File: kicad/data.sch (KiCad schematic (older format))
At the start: 58 parts, among them J2 USB_B, J3 FTDI header, J4 PTT choice, J5 XCVR_CAT_TTL, J6 XCVR_PTT, U3 SN65220, U4 Si8663AB-B-IS1, U5 FT232RL, U6 SN74HCT32D, U7 VOR1121B6T

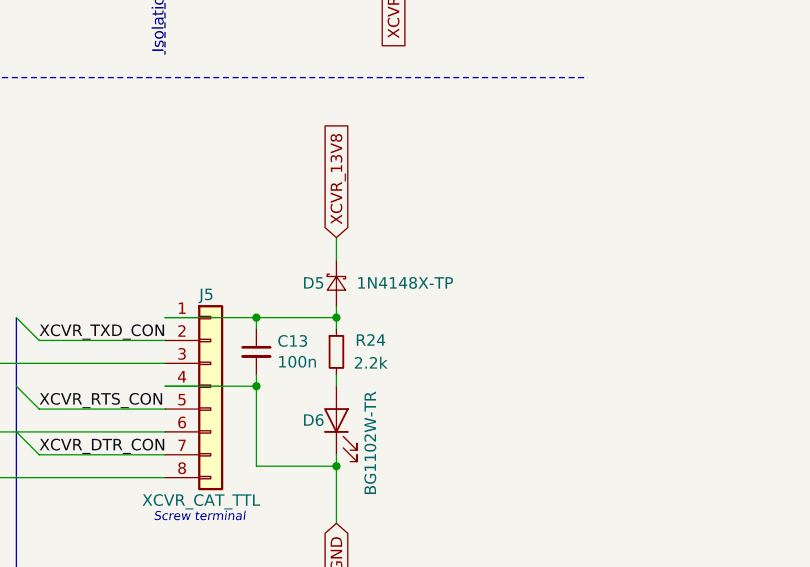
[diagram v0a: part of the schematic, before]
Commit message: Small fixes
* Moved via that was unreasonably close to another one
* Changed 13V8 diodes to SM5819PL-TP
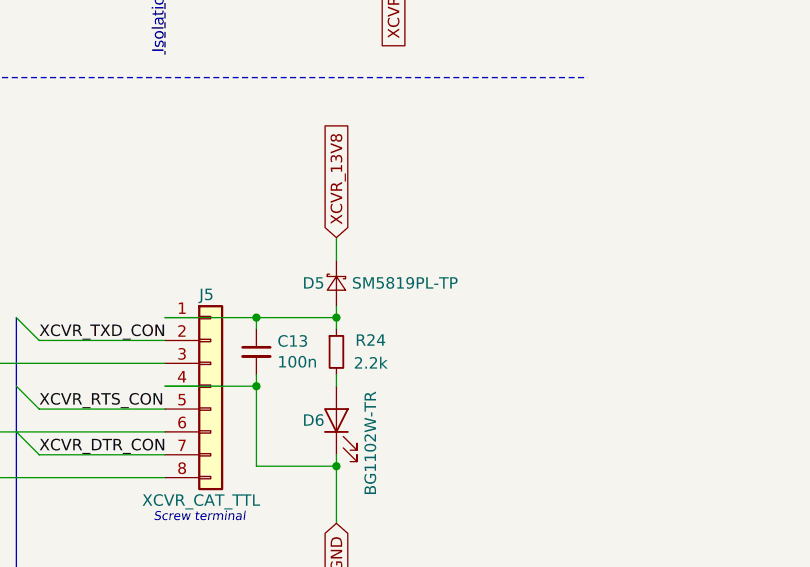
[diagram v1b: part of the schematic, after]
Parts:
- D5: value 1N4148X-TP -> SM5819PL-TP; footprint Diode_SMD:D_SOD-523 -> Diode_SMD:D_SOD-123F
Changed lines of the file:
@@
 P 10100 2900
 F 0 "D5" V 10100 3000 50  0000 C CNN
-F 1 "1N4148X-TP" V 10100 2600 50  0000 C CNN
-F 2 "Diode_SMD:D_SOD-523" V 10100 2900 50  0001 C CNN
+F 1 "SM5819PL-TP" V 10100 2600 50  0000 C CNN
+F 2 "Diode_SMD:D_SOD-123F" V 10100 2900 50  0001 C CNN
 F 3 "~" V 10100 2900 50  0001 C CNN
 	1    10100 2900

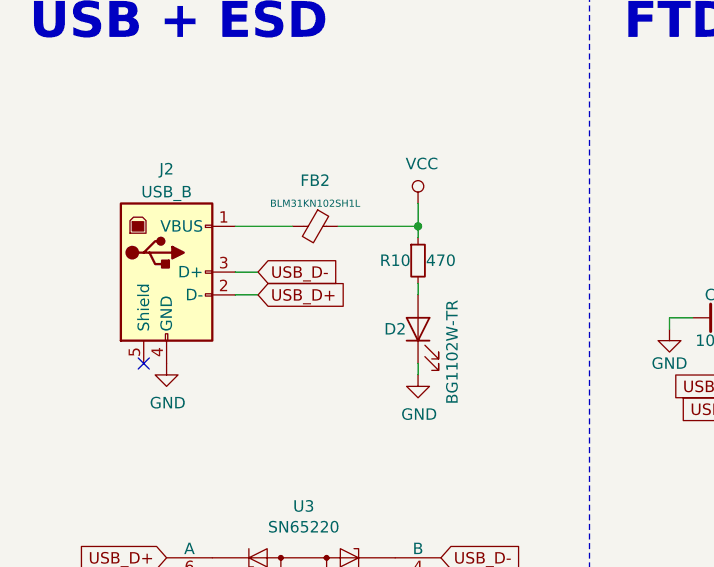
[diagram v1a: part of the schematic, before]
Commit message: Bugfixes
* Fixed USB D+/D- switch
* Added clearance at top right mounting hole
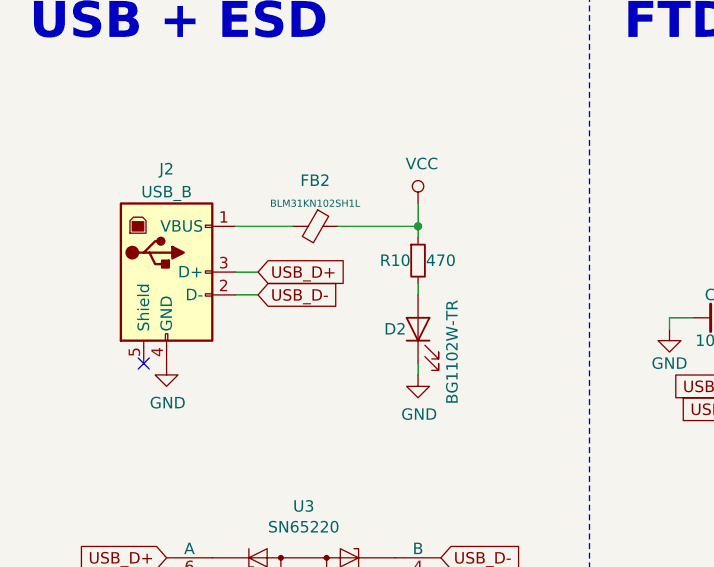
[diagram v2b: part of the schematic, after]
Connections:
- net USB_D+: now also J2.3 (D+); no longer J2.2 (D-)
- net USB_D-: now also J2.2 (D-); no longer J2.3 (D+)
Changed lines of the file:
@@
 Comment4 ""
 $EndDescr
-Text GLabel 1550 1750 2    50   Input ~ 0
+Text GLabel 1550 1850 2    50   Input ~ 0
 USB_D-
 $Comp
@@
 	1    0    0    -1
 $EndComp
-Text GLabel 1550 1850 2    50   Input ~ 0
+Text GLabel 1550 1750 2    50   Input ~ 0
 USB_D+
 $Comp
